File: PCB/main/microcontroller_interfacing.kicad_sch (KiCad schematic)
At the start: 0 parts

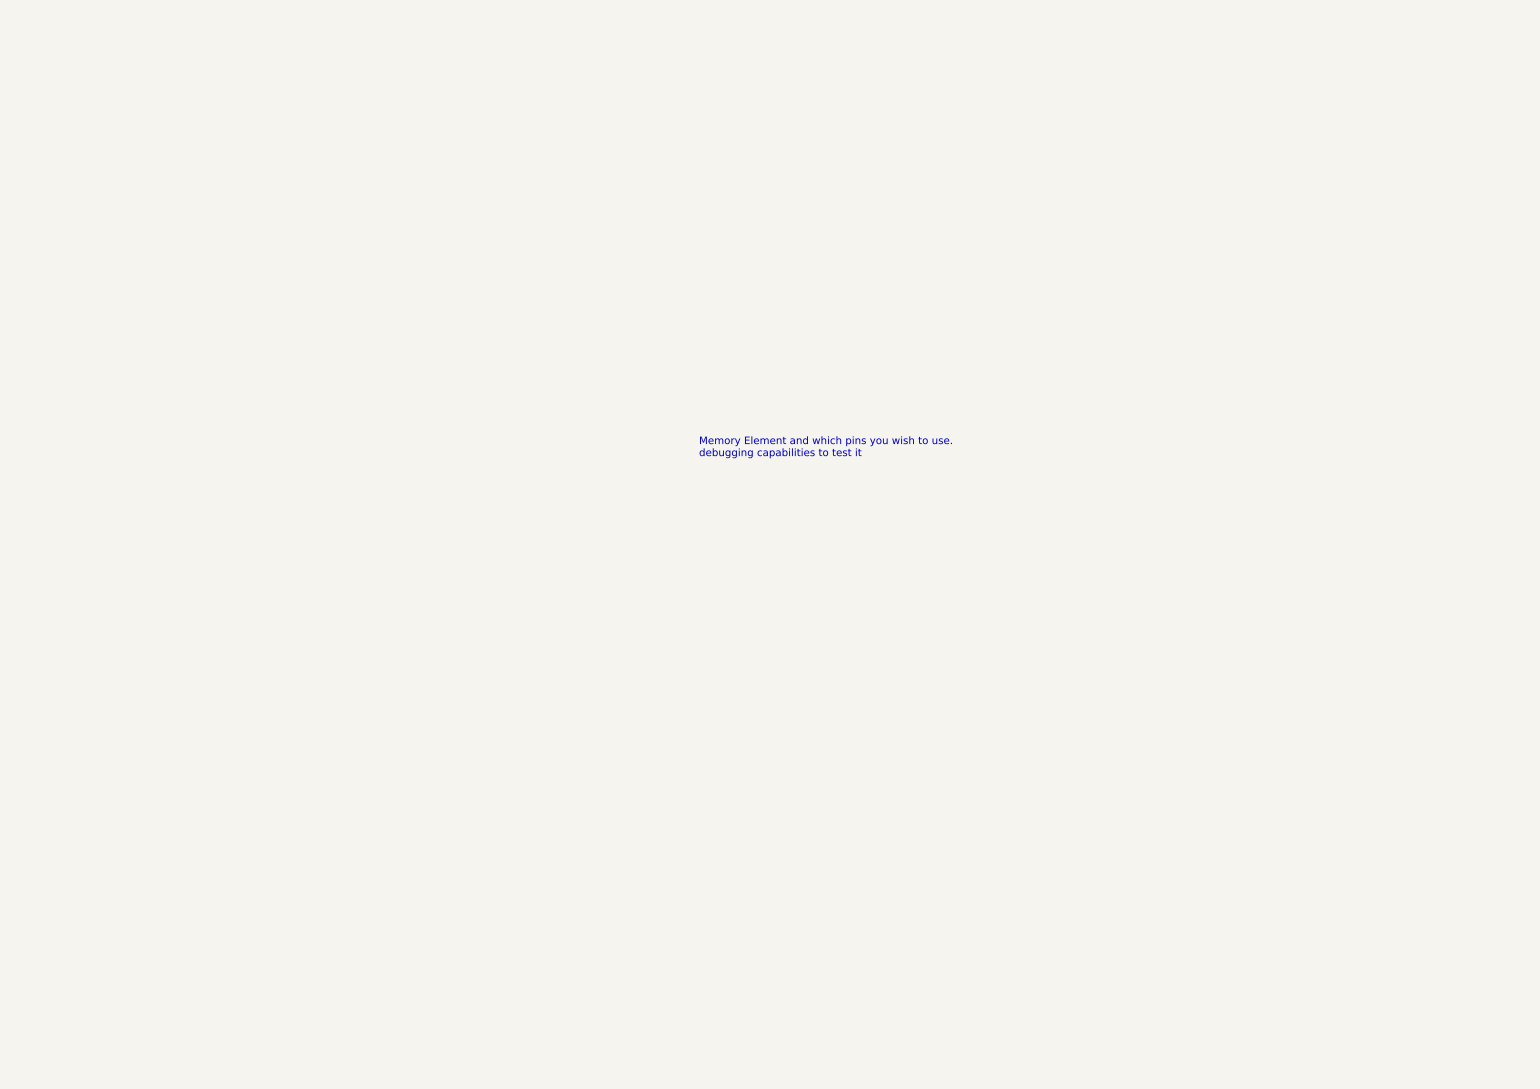
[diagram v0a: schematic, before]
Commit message: power and microcontroller updated
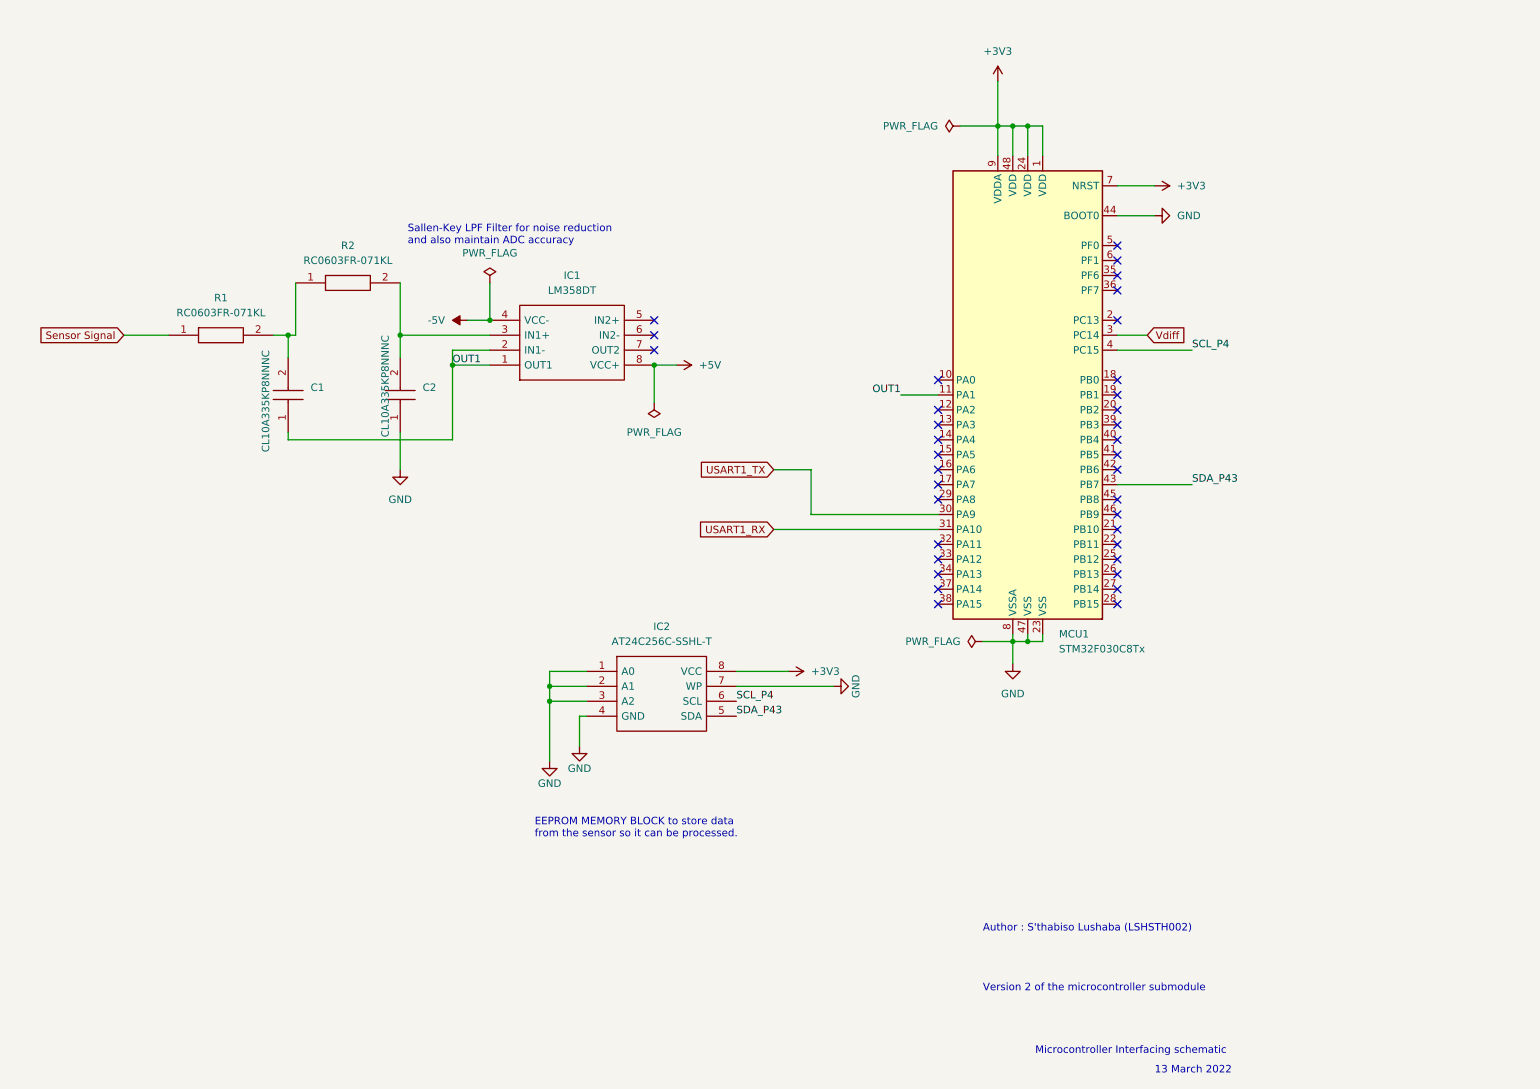
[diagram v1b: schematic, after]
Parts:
- added C1, C2: CL10A335KP8NNNC, SamacSys_Parts:CAPC1608X90N, symbol SamacSys_Parts_Microcontroller:CL10A335KP8NNNC
- added IC1: LM358DT, SamacSys_Parts:SOIC127P600X175-8N, symbol SamacSys_Parts:LM358DT
- added IC2: AT24C256C-SSHL-T, SamacSys_Parts:SOIC127P600X175-8N, symbol SamacSys_Parts_Microcontroller:AT24C256C-SSHL-T
- added MCU1: STM32F030C8Tx, Package_QFP:LQFP-48_7x7mm_P0.5mm, symbol MCU_ST_STM32F0:STM32F030C8Tx
- added R1, R2: RC0603FR-071KL, SamacSys_Parts:RESC1608X55N, symbol SamacSys_Parts_Microcontroller:RC0603FR-071KL
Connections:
- new net: C2.2, IC1.3 (IN1+), R2.2
- new net: C1.2, R1.2, R2.1
- new net +3V3: IC2.8 (VCC), MCU1.1 (VDD), MCU1.24 (VDD), MCU1.48 (VDD), MCU1.7 (NRST), MCU1.9 (VDDA)
- new net +5V: IC1.8 (VCC+)
- new net -5V: IC1.4 (VCC-)
- new net GND: C2.1, IC2.1 (A0), IC2.2 (A1), IC2.3 (A2), IC2.4 (GND), IC2.7 (WP), MCU1.23 (VSS), MCU1.44 (BOOT0), MCU1.47 (VSS), MCU1.8 (VSSA)
- new net OUT1: C1.1, IC1.1 (OUT1), IC1.2 (IN1-), MCU1.11 (PA1)
- new net SCL_P4: IC2.6 (SCL), MCU1.4 (PC15)
- new net SDA_P43: IC2.5 (SDA), MCU1.43 (PB7)
- new net Sensor Signal: R1.1
- new net USART1_RX: MCU1.31 (PA10)
- new net USART1_TX: MCU1.30 (PA9)
- new net Vdiff: MCU1.3 (PC14)
- no-connect marks 0 -> 36
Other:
- note added: "13 March 2022"
- note added: "Author : S'thabiso Lushaba (LSHSTH002)"
- note added: "EEPROM MEMORY BLOCK to store data from the sensor so it can be processed."
- note added: "Microcontroller Interfacing schematic"
- note added: "Sallen-Key LPF Filter for noise reduction and also maintain ADC accuracy"
- note added: "Version 2 of the microcontroller submodule"
- note removed: "Memory Element and which pins you wish to use. debugging capabilities to test it"

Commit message: changes made to all
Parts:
- renumbered C1 to C11, C2 to C12, IC1 to IC2, IC2 to IC3, R1 to R12, R2 to R13
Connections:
- net +3V3 renamed Vsupply
- net +5V renamed +3v3
- net -5V renamed -3v3
- net Sensor Signal renamed Vout1

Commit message: git main schematics updated
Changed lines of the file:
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@@
   (junction (at 182.88 33.02) (diameter 0) (color 0 0 0 0)
   )
-  (junction (at 93.98 66.04) (diameter 0) (color 0 0 0 0)
-  )
   (junction (at 59.69 68.58) (diameter 0) (color 0 0 0 0)
   )
+  (junction (at 104.14 133.35) (diameter 0) (color 0 0 0 0)
+  )
   (junction (at 185.42 33.02) (diameter 0) (color 0 0 0 0)
   )
+  (junction (at 110.49 133.35) (diameter 0) (color 0 0 0 0)
+  )
   (junction (at 185.42 120.65) (diameter 0) (color 0 0 0 0)
-  )
-  (junction (at 121.92 73.66) (diameter 0) (color 0 0 0 0)
   )
   (junction (at 182.88 120.65) (diameter 0) (color 0 0 0 0)
@@
     (stroke (width 0) (type default) (color 0 0 0 0))
   )
+  (wire (pts (xy 104.14 133.35) (xy 110.49 133.35))
+    (stroke (width 0) (type default) (color 0 0 0 0))
+  )
   (wire (pts (xy 104.14 125.73) (xy 104.14 128.27))
     (stroke (width 0) (type default) (color 0 0 0 0))
@@
     (stroke (width 0) (type default) (color 0 0 0 0))
   )
+  (wire (pts (xy 110.49 133.35) (xy 110.49 137.16))
+    (stroke (width 0) (type default) (color 0 0 0 0))
+  )
   (wire (pts (xy 87.63 73.66) (xy 87.63 71.12))
     (stroke (width 0) (type default) (color 0 0 0 0))
@@
     (stroke (width 0) (type default) (color 0 0 0 0))
   )
-  (wire (pts (xy 173.99 33.02) (xy 180.34 33.02))
-    (stroke (width 0) (type default) (color 0 0 0 0))
-  )
-  (wire (pts (xy 104.14 130.81) (xy 104.14 140.97))
+  (wire (pts (xy 104.14 130.81) (xy 104.14 133.35))
     (stroke (width 0) (type default) (color 0 0 0 0))
   )
@@
     (stroke (width 0) (type default) (color 0 0 0 0))
   )
-  (wire (pts (xy 109.22 133.35) (xy 109.22 138.43))
-    (stroke (width 0) (type default) (color 0 0 0 0))
-  )
   (wire (pts (xy 87.63 86.36) (xy 87.63 73.66))
     (stroke (width 0) (type default) (color 0 0 0 0))
@@
     (stroke (width 0) (type default) (color 0 0 0 0))
   )
-  (wire (pts (xy 177.8 120.65) (xy 182.88 120.65))
-    (stroke (width 0) (type default) (color 0 0 0 0))
-  )
   (wire (pts (xy 187.96 38.1) (xy 187.96 33.02))
     (stroke (width 0) (type default) (color 0 0 0 0))
@@
     (stroke (width 0) (type default) (color 0 0 0 0))
   )
-  (wire (pts (xy 121.92 73.66) (xy 121.92 80.01))
-    (stroke (width 0) (type default) (color 0 0 0 0))
-  )
   (wire (pts (xy 200.66 48.26) (xy 207.01 48.26))
     (stroke (width 0) (type default) (color 0 0 0 0))
@@
     (stroke (width 0) (type default) (color 0 0 0 0))
   )
+  (wire (pts (xy 104.14 133.35) (xy 104.14 140.97))
+    (stroke (width 0) (type default) (color 0 0 0 0))
+  )
   (wire (pts (xy 135.89 128.27) (xy 152.4 128.27))
     (stroke (width 0) (type default) (color 0 0 0 0))
@@
   )
   (wire (pts (xy 182.88 33.02) (xy 182.88 38.1))
-    (stroke (width 0) (type default) (color 0 0 0 0))
-  )
-  (wire (pts (xy 93.98 59.69) (xy 93.98 66.04))
-    (stroke (width 0) (type default) (color 0 0 0 0))
-  )
-  (wire (pts (xy 110.49 133.35) (xy 109.22 133.35))
     (stroke (width 0) (type default) (color 0 0 0 0))
   )
@@
     (pin "1")
     (pin "2")
-  )
-  (symbol (lib_id "power:PWR_FLAG") (at 121.92 80.01 180) (unit 1)
-    (in_bom yes) (on_board yes) (fields_autoplaced)
-    (property "Reference" "#FLG07" (id 0) (at 121.92 81.915 0)
-      (effects (font (size 1.27 1.27)) hide)
-    )
-    (property "Value" "PWR_FLAG" (id 1) (at 121.92 85.09 0))
-    (property "Footprint" "" (id 2) (at 121.92 80.01 0)
-      (effects (font (size 1.27 1.27)) hide)
-    )
-    (property "Datasheet" "~" (id 3) (at 121.92 80.01 0)
-      (effects (font (size 1.27 1.27)) hide)
-    )
-    (pin "1")
   )
   (symbol (lib_id "SamacSys_Parts_Microcontroller:RC0603FR-071KL") (at 60.96 59.69 0) (unit 1)
@@
     (pin "8")
   )
-  (symbol (lib_id "power:PWR_FLAG") (at 93.98 59.69 0) (unit 1)
+  (symbol (lib_id "power:PWR_FLAG") (at 110.49 137.16 180) (unit 1)
     (in_bom yes) (on_board yes) (fields_autoplaced)
-    (property "Reference" "#FLG06" (id 0) (at 93.98 57.785 0)
-      (effects (font (size 1.27 1.27)) hide)
-    )
-    (property "Value" "PWR_FLAG" (id 1) (at 93.98 54.61 0))
-    (property "Footprint" "" (id 2) (at 93.98 59.69 0)
-      (effects (font (size 1.27 1.27)) hide)
-    )
-    (property "Datasheet" "~" (id 3) (at 93.98 59.69 0)
-      (effects (font (size 1.27 1.27)) hide)
-    )
-    (pin "1")
-  )
-  (symbol (lib_id "power:PWR_FLAG") (at 173.99 33.02 90) (unit 1)
-    (in_bom yes) (on_board yes) (fields_autoplaced)
-    (property "Reference" "#FLG08" (id 0) (at 172.085 33.02 0)
-      (effects (font (size 1.27 1.27)) hide)
-    )
-    (property "Value" "PWR_FLAG" (id 1) (at 170.18 33.0199 90)
-      (effects (font (size 1.27 1.27)) (justify left))
-    )
-    (property "Footprint" "" (id 2) (at 173.99 33.02 0)
-      (effects (font (size 1.27 1.27)) hide)
-    )
-    (property "Datasheet" "~" (id 3) (at 173.99 33.02 0)
+    (property "Reference" "#FLG0103" (id 0) (at 110.49 139.065 0)
+      (effects (font (size 1.27 1.27)) hide)
+    )
+    (property "Value" "PWR_FLAG" (id 1) (at 110.49 142.24 0))
+    (property "Footprint" "" (id 2) (at 110.49 137.16 0)
+      (effects (font (size 1.27 1.27)) hide)
+    )
+    (property "Datasheet" "~" (id 3) (at 110.49 137.16 0)
       (effects (font (size 1.27 1.27)) hide)
     )
@@
     )
     (property "Datasheet" "" (id 3) (at 182.88 124.46 0)
-      (effects (font (size 1.27 1.27)) hide)
-    )
-    (pin "1")
-  )
-  (symbol (lib_id "power:PWR_FLAG") (at 177.8 120.65 90) (unit 1)
-    (in_bom yes) (on_board yes) (fields_autoplaced)
-    (property "Reference" "#FLG09" (id 0) (at 175.895 120.65 0)
-      (effects (font (size 1.27 1.27)) hide)
-    )
-    (property "Value" "PWR_FLAG" (id 1) (at 173.99 120.6499 90)
-      (effects (font (size 1.27 1.27)) (justify left))
-    )
-    (property "Footprint" "" (id 2) (at 177.8 120.65 0)
-      (effects (font (size 1.27 1.27)) hide)
-    )
-    (property "Datasheet" "~" (id 3) (at 177.8 120.65 0)
       (effects (font (size 1.27 1.27)) hide)
     )
@@
       (effects (font (size 1.27 1.27)) hide)
     )
-    (pin "1")
-  )
-  (symbol (lib_id "power:GND") (at 109.22 138.43 0) (unit 1)
-    (in_bom yes) (on_board yes)
-    (property "Reference" "#PWR038" (id 0) (at 109.22 144.78 0)
-      (effects (font (size 1.27 1.27)) hide)
-    )
-    (property "Value" "GND" (id 1) (at 109.22 142.24 0))
-    (property "Footprint" "" (id 2) (at 109.22 138.43 0)
-      (effects (font (size 1.27 1.27)) hide)
-    )
-    (property "Datasheet" "" (id 3) (at 109.22 138.43 0)
-      (effects (font (size 1.27 1.27)) hide)
-    )

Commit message: latest changes
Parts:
- added TP? (x2): TestPoint, symbol Connector:TestPoint
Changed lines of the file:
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@@
+    (pin "1")
+  )
+  (symbol (lib_id "Connector:TestPoint") (at 92.71 66.04 0) (unit 1)
+    (in_bom yes) (on_board yes) (fields_autoplaced)
+    (property "Reference" "TP?" (id 0) (at 95.25 61.4679 0)
+      (effects (font (size 1.27 1.27)) (justify left))
+    )
+    (property "Value" "TestPoint" (id 1) (at 95.25 64.0079 0)
+      (effects (font (size 1.27 1.27)) (justify left))
+    )
+    (property "Footprint" "" (id 2) (at 97.79 66.04 0)
+      (effects (font (size 1.27 1.27)) hide)
+    )
+    (property "Datasheet" "~" (id 3) (at 97.79 66.04 0)
+      (effects (font (size 1.27 1.27)) hide)
+    )
     (pin "1")
   )
@@
     (pin "2")
   )
+  (symbol (lib_id "Connector:TestPoint") (at 124.46 73.66 180) (unit 1)
+    (in_bom yes) (on_board yes) (fields_autoplaced)
+    (property "Reference" "TP?" (id 0) (at 127 75.6919 0)
+      (effects (font (size 1.27 1.27)) (justify right))
+    )
+    (property "Value" "TestPoint" (id 1) (at 127 78.2319 0)
+      (effects (font (size 1.27 1.27)) (justify right))
+    )
+    (property "Footprint" "" (id 2) (at 119.38 73.66 0)
+      (effects (font (size 1.27 1.27)) hide)
+    )
+    (property "Datasheet" "~" (id 3) (at 119.38 73.66 0)
+      (effects (font (size 1.27 1.27)) hide)
+    )
+    (pin "1")
+  )
   (symbol (lib_id "SamacSys_Parts_Microcontroller:AT24C256C-SSHL-T") (at 110.49 125.73 0) (unit 1)
